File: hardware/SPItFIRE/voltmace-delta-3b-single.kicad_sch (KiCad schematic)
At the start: 6 parts

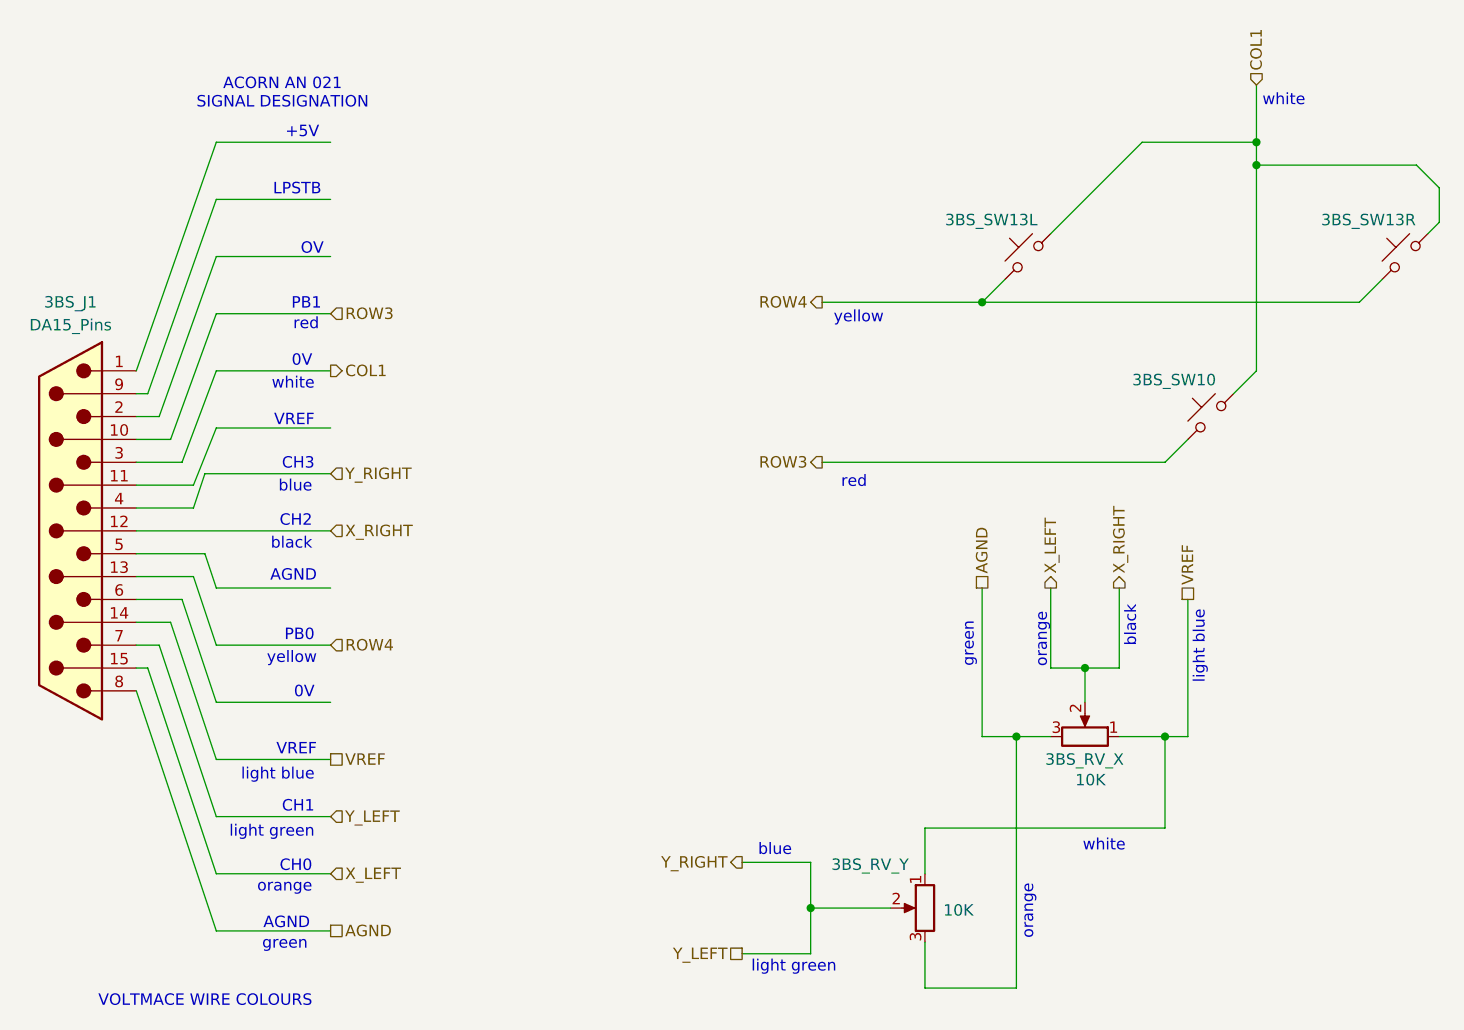
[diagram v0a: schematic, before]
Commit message: Update schematic naming convention to keep Kicad happy
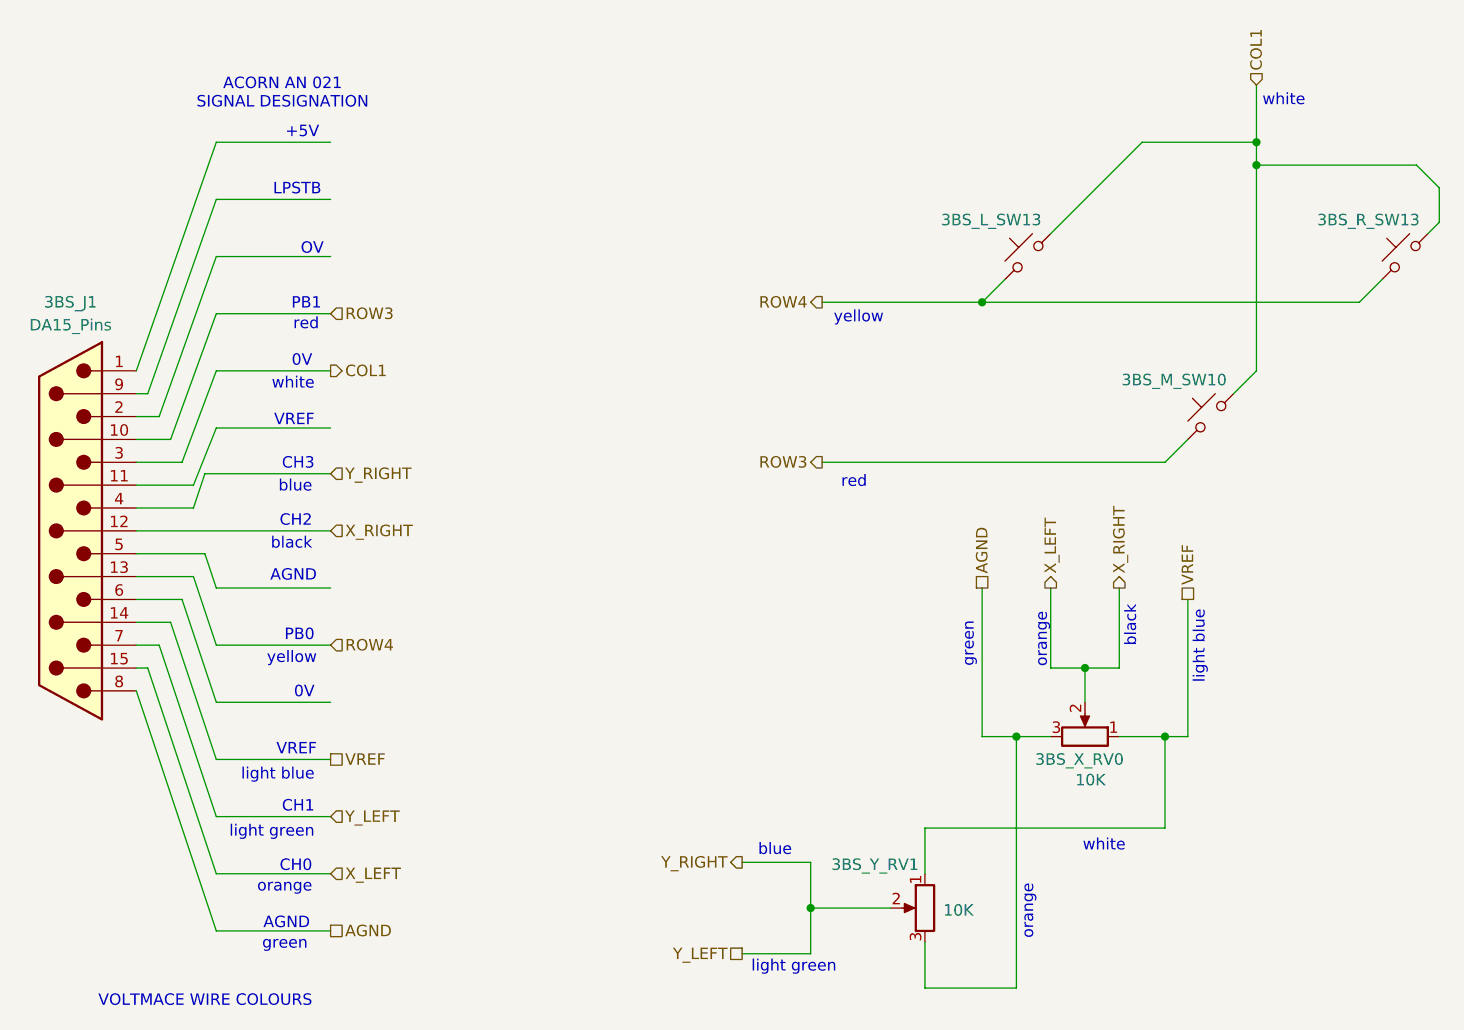
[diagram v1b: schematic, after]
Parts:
- renumbered 3BS_SW13L to 3BS_L_SW13, 3BS_SW10 to 3BS_M_SW10, 3BS_SW13R to 3BS_R_SW13, 3BS_RV_X to 3BS_X_RV0, 3BS_RV_Y to 3BS_Y_RV1
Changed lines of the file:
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@@
+				)
+			)
+			(project "voltmace-delta-3b-single"
+				(path "/f967801f-4cfb-4170-805d-07c01398a82e"
+					(reference "3BS_J1")
+					(unit 1)
 				)
 			)
@@
 		(on_board yes)
 		(dnp no)
-		(property "Reference" "3BS_RV_Y"
+		(property "Reference" "3BS_Y_RV1"
 			(at 141.986 150.114 0)
 			(effects
@@
 				(path "/148e0ceb-efca-48fe-9d35-9803ba402dc8/1cc94f17-3819-4fc0-9e35-99596cc7197b"
 					(reference "3BS_RV_Y")
+					(unit 1)
+				)
+			)
+			(project "voltmace-delta-3b-single"
+				(path "/f967801f-4cfb-4170-805d-07c01398a82e"
+					(reference "3BS_Y_RV1")
 					(unit 1)
 				)
@@
 		(on_board yes)
 		(dnp no)
-		(property "Reference" "3BS_SW13L"
+		(property "Reference" "3BS_L_SW13"
 			(at 159.766 78.486 0)
 			(effects
@@
 				(path "/148e0ceb-efca-48fe-9d35-9803ba402dc8/1cc94f17-3819-4fc0-9e35-99596cc7197b"
 					(reference "3BS_SW13L")
+					(unit 1)
+				)
+			)
+			(project "voltmace-delta-3b-single"
+				(path "/f967801f-4cfb-4170-805d-07c01398a82e"
+					(reference "3BS_L_SW13")
 					(unit 1)
 				)
@@
 		(on_board yes)
 		(dnp no)
-		(property "Reference" "3BS_RV_X"
+		(property "Reference" "3BS_X_RV0"
 			(at 174.498 138.43 90)
 			(effects
@@
 				(path "/148e0ceb-efca-48fe-9d35-9803ba402dc8/1cc94f17-3819-4fc0-9e35-99596cc7197b"
 					(reference "3BS_RV_X")
+					(unit 1)
+				)
+			)
+			(project "voltmace-delta-3b-single"
+				(path "/f967801f-4cfb-4170-805d-07c01398a82e"
+					(reference "3BS_X_RV0")
 					(unit 1)
 				)
@@
 		(on_board yes)
 		(dnp no)
-		(property "Reference" "3BS_SW10"
+		(property "Reference" "3BS_M_SW10"
 			(at 180.086 96.266 0)
 			(effects
@@
 				(path "/148e0ceb-efca-48fe-9d35-9803ba402dc8/1cc94f17-3819-4fc0-9e35-99596cc7197b"
 					(reference "3BS_SW10")
+					(unit 1)
+				)
+			)
+			(project "voltmace-delta-3b-single"
+				(path "/f967801f-4cfb-4170-805d-07c01398a82e"
+					(reference "3BS_M_SW10")
 					(unit 1)
 				)
@@
 		(on_board yes)
 		(dnp no)
-		(property "Reference" "3BS_SW13R"
+		(property "Reference" "3BS_R_SW13"
 			(at 201.676 78.486 0)
 			(effects
@@
 				)
 			)
-		)
-	)
+			(project "voltmace-delta-3b-single"
+				(path "/f967801f-4cfb-4170-805d-07c01398a82e"
+					(reference "3BS_R_SW13")
+					(unit 1)
+				)
+			)
+		)
+	)
+	(sheet_instances
+		(path "/"
+			(page "1")
+		)
+	)
+	(embedded_fonts no)
 )

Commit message: The bulk of the schematic layout for the board (pending review and check)
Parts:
- renumbered 3BS_X_RV0 to 3BS_RV_X, 3BS_Y_RV1 to 3BS_RV_Y, 3BS_M_SW10 to 3BS_SW10, 3BS_L_SW13 to 3BS_SW13L, 3BS_R_SW13 to 3BS_SW13R

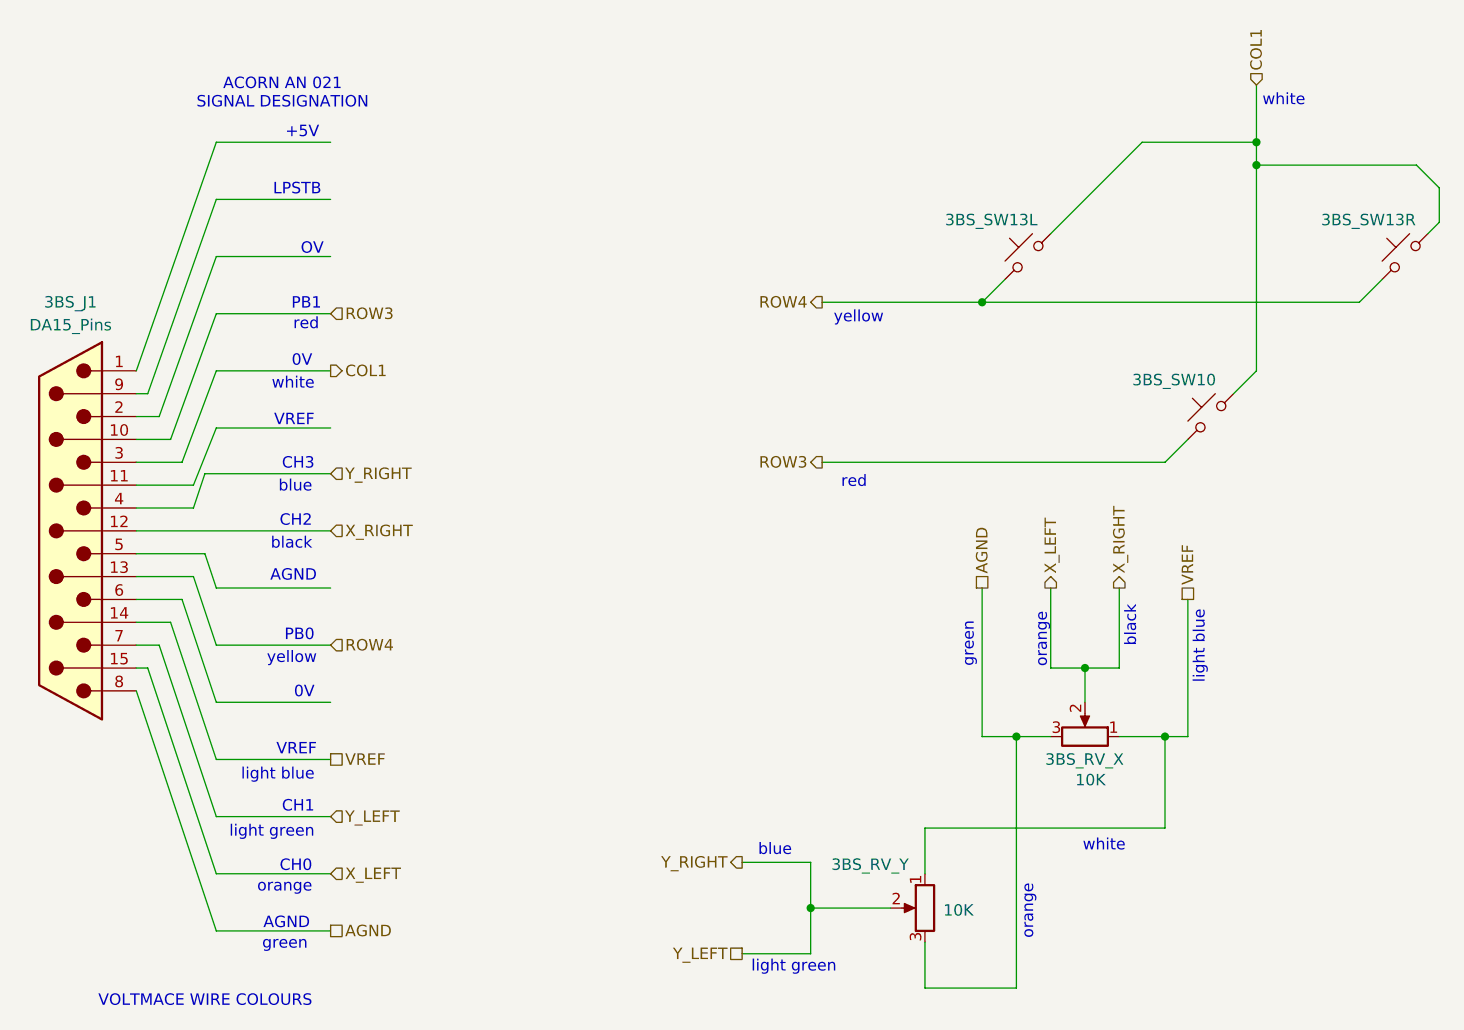
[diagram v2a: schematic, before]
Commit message: Schematic updates and rule checking
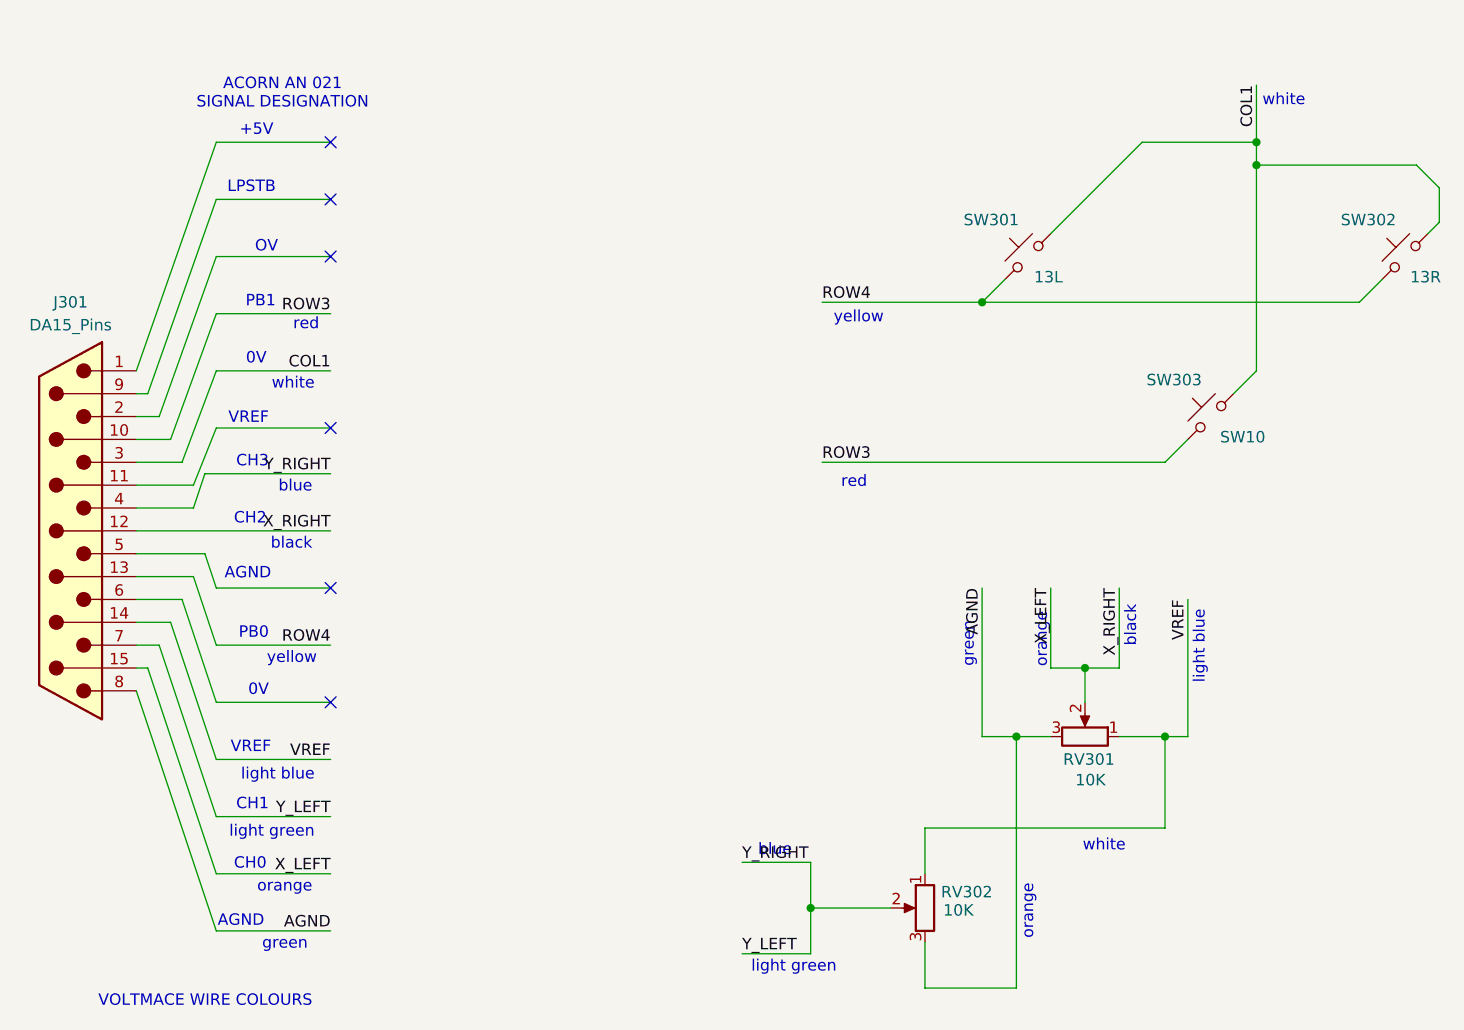
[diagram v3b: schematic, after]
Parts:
- SW301: renamed from 3BS_SW13L; value SW_Push_45deg -> 13L
- SW302: renamed from 3BS_SW13R; value SW_Push_45deg -> 13R
- SW303: renamed from 3BS_SW10; value SW_Push_45deg -> SW10
- renumbered 3BS_J1 to J301, 3BS_RV_X to RV301, 3BS_RV_Y to RV302
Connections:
- no-connect marks 0 -> 6
